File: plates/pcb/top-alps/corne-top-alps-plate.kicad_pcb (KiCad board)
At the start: 2 copper layers, 132.9 x 91.4 mm, 28 parts, among them SW2 KEY_SWITCH

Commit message: plates
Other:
- net class Default removed

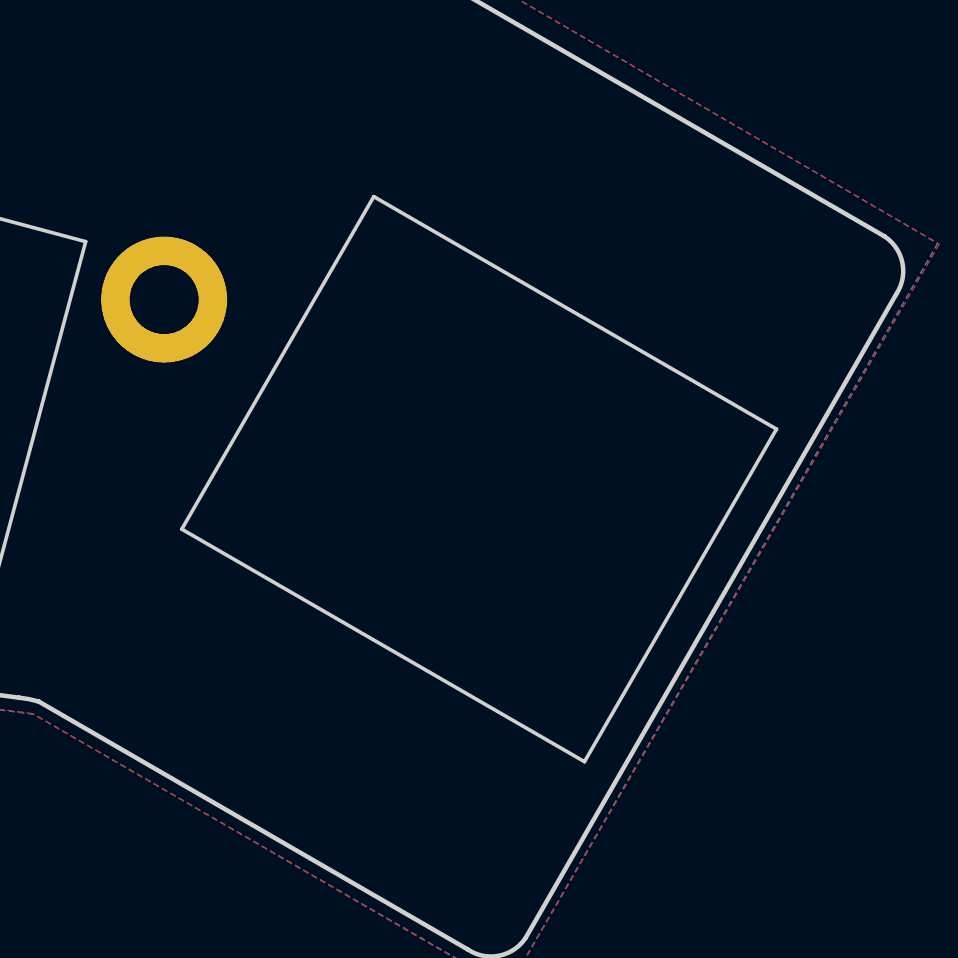
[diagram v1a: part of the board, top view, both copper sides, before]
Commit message: Fix the thumb key for alps pcb plate
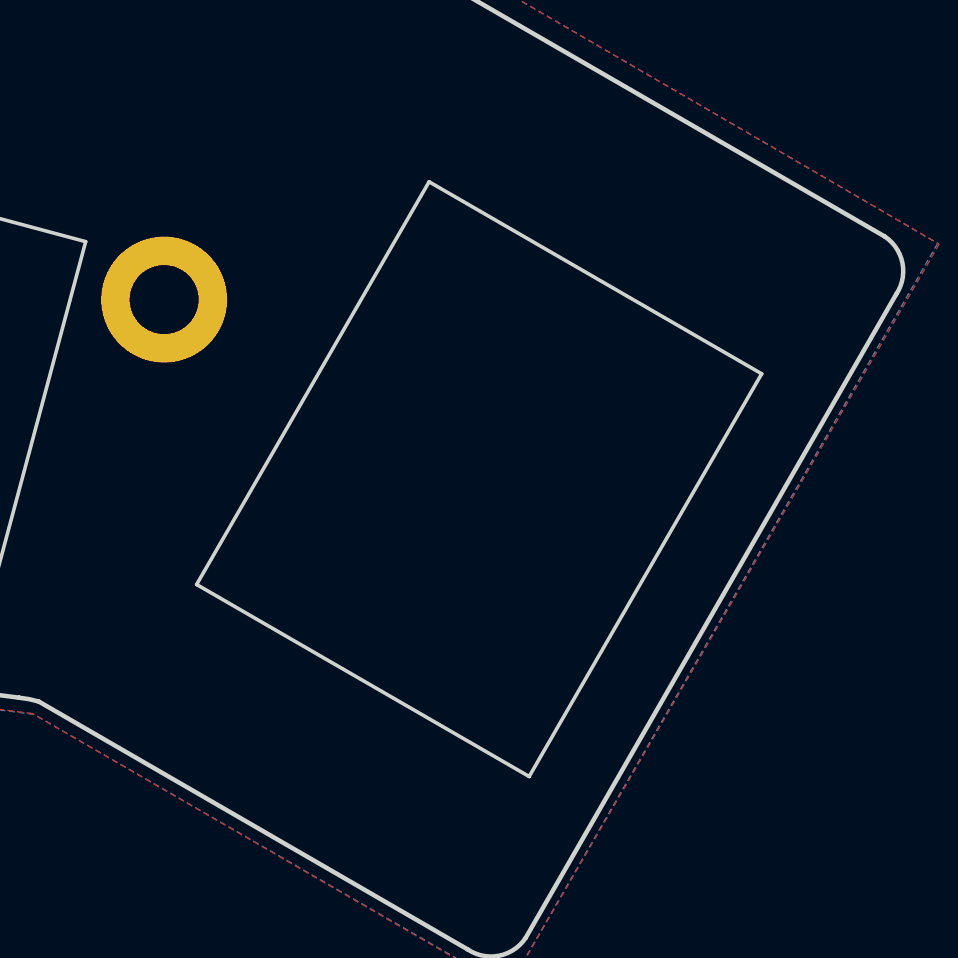
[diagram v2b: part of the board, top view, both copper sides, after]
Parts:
- turned SW2 to -120 degrees
